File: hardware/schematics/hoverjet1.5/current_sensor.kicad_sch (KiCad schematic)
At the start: 6 parts, among them J5 -VIN, J6 +VIN, J7 Conn_01x06

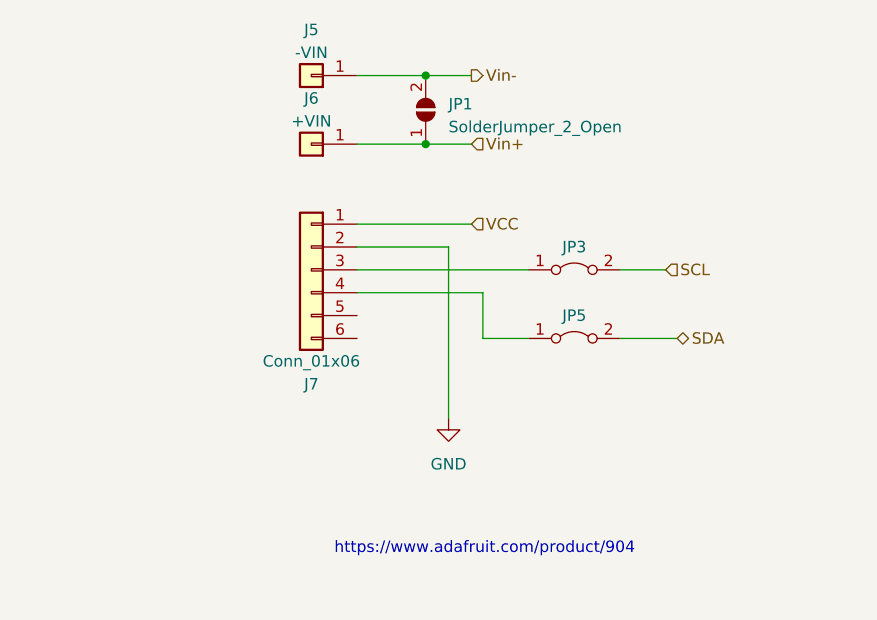
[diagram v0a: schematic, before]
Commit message: added adafruit current sense breakout
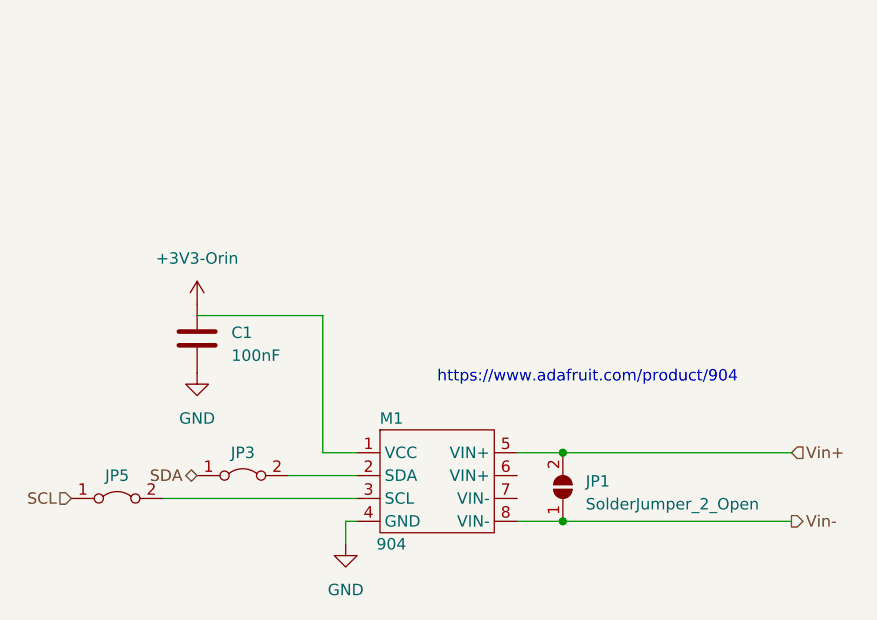
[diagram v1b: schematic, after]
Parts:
- removed J5: -VIN, symbol Connector_Generic:Conn_01x01
- removed J6: +VIN, symbol Connector_Generic:Conn_01x01
- removed J7: Conn_01x06, symbol Connector_Generic:Conn_01x06
- added C1: 100nF, Capacitor_SMD:C_0201_0603Metric, symbol Device:C
- added M1: 904, symbol hoverjet:904
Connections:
- net GND: now also C1.2, M1.4 (GND)
- net SCL: now also JP5.1 (A); no longer JP3.2 (B)
- net SDA: now also JP3.1 (A); no longer JP5.2 (B)
- net Vin+: now also JP1.2 (B), M1.5 (VIN+); no longer JP1.1 (A)
- net Vin-: now also JP1.1 (A), M1.8 (VIN-); no longer JP1.2 (B)
- new net: JP3.2 (B), M1.2 (SDA)
- new net: JP5.2 (B), M1.3 (SCL)
- new net +3V3-Orin: C1.1
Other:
- moved on the sheet: JP1, JP3, JP5

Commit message: syncing hardware changes
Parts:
- removed C1: 100nF, Capacitor_SMD:C_0201_0603Metric, symbol Device:C
- removed JP1: SolderJumper_2_Open, Jumper:SolderJumper-2_P1.3mm_Open_RoundedPad1.0x1.5mm, symbol Jumper:SolderJumper_2_Open
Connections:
- net +3V3-Orin: now also M1.1 (VCC)
- net Vin+: now also M1.6 (VIN+)
- net Vin-: now also M1.7 (VIN-)
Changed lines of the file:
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@@
 (kicad_sch (version 20230121) (generator eeschema)
   (paper "A4")
-  (junction (at 152.4 100.33) (diameter 0) (color 0 0 0 0)
+  (junction (at 151.13 100.33) (diameter 0) (color 0 0 0 0)
   )
-  (junction (at 152.4 107.95) (diameter 0) (color 0 0 0 0)
+  (junction (at 151.13 107.95) (diameter 0) (color 0 0 0 0)
+  )
+  (wire (pts (xy 151.13 100.33) (xy 177.8 100.33))
+    (stroke (width 0) (type default))
   )
   (wire (pts (xy 121.92 102.87) (xy 129.54 102.87))
     (stroke (width 0) (type default))
   )
-  (wire (pts (xy 111.76 85.09) (xy 125.73 85.09))
+  (wire (pts (xy 147.32 107.95) (xy 151.13 107.95))
     (stroke (width 0) (type default))
   )
-  (wire (pts (xy 147.32 107.95) (xy 152.4 107.95))
+  (wire (pts (xy 151.13 105.41) (xy 151.13 107.95))
+    (stroke (width 0) (type default))
+  )
+  (wire (pts (xy 147.32 102.87) (xy 151.13 102.87))
+    (stroke (width 0) (type default))
+  )
+  (wire (pts (xy 147.32 105.41) (xy 151.13 105.41))
     (stroke (width 0) (type default))
   )
@@
     (stroke (width 0) (type default))
   )
-  (wire (pts (xy 147.32 100.33) (xy 152.4 100.33))
+  (wire (pts (xy 147.32 100.33) (xy 151.13 100.33))
     (stroke (width 0) (type default))
   )
-  (wire (pts (xy 152.4 107.95) (xy 177.8 107.95))
+  (wire (pts (xy 151.13 107.95) (xy 177.8 107.95))
     (stroke (width 0) (type default))
   )
-  (wire (pts (xy 125.73 85.09) (xy 125.73 100.33))
+  (wire (pts (xy 151.13 100.33) (xy 151.13 102.87))
     (stroke (width 0) (type default))
   )
   (wire (pts (xy 107.95 105.41) (xy 129.54 105.41))
-    (stroke (width 0) (type default))
-  )
-  (wire (pts (xy 152.4 100.33) (xy 177.8 100.33))
     (stroke (width 0) (type default))
   )
@@
     )
   )
-  (symbol (lib_id "power:GND") (at 111.76 91.44 0) (unit 1)
+  (symbol (lib_id "hoverjet:+3V3-Orin") (at 125.73 100.33 0) (unit 1)
     (in_bom yes) (on_board yes) (dnp no) (fields_autoplaced)
-    (property "Reference" "#PWR08" (at 111.76 97.79 0)
+    (property "Reference" "#PWR019" (at 125.73 104.14 0)
       (effects (font (size 1.27 1.27)) hide)
     )
-    (property "Value" "GND" (at 111.76 96.52 0)
+    (property "Value" "+3V3-Orin" (at 125.73 95.25 0)
       (effects (font (size 1.27 1.27)))
     )
-    (property "Footprint" "" (at 111.76 91.44 0)
+    (property "Footprint" "" (at 125.73 100.33 0)
       (effects (font (size 1.27 1.27)) hide)
     )
-    (property "Datasheet" "" (at 111.76 91.44 0)
-      (effects (font (size 1.27 1.27)) hide)
-    )
-    (pin "1")
-    (instances
-      (project "hoverjet1.5"
-        (path "/667b3107-350e-4594-8aa7-7f2b7bfa6370/61ccea04-2db4-419f-a542-3a277e457f40/b686100f-0650-40a5-8577-84613a1e214b"
-          (reference "#PWR08") (unit 1)
-        )
-        (path "/667b3107-350e-4594-8aa7-7f2b7bfa6370/61ccea04-2db4-419f-a542-3a277e457f40/a21bb2a3-fb47-48f7-9a11-9f63725ae484"
-          (reference "#PWR014") (unit 1)
-        )
-      )
-    )
-  )
-  (symbol (lib_id "hoverjet:+3V3-Orin") (at 111.76 83.82 0) (unit 1)
-    (in_bom yes) (on_board yes) (dnp no) (fields_autoplaced)
-    (property "Reference" "#PWR019" (at 111.76 87.63 0)
-      (effects (font (size 1.27 1.27)) hide)
-    )
-    (property "Value" "+3V3-Orin" (at 111.76 78.74 0)
-      (effects (font (size 1.27 1.27)))
-    )
-    (property "Footprint" "" (at 111.76 83.82 0)
-      (effects (font (size 1.27 1.27)) hide)
-    )
-    (property "Datasheet" "" (at 111.76 83.82 0)
+    (property "Datasheet" "" (at 125.73 100.33 0)
       (effects (font (size 1.27 1.27)) hide)
     )
@@
     )
   )
-  (symbol (lib_id "Jumper:SolderJumper_2_Open") (at 152.4 104.14 90) (unit 1)
-    (in_bom yes) (on_board yes) (dnp no) (fields_autoplaced)
-    (property "Reference" "JP1" (at 154.94 103.505 90)
-      (effects (font (size 1.27 1.27)) (justify right))
-    )
-    (property "Value" "SolderJumper_2_Open" (at 154.94 106.045 90)
-      (effects (font (size 1.27 1.27)) (justify right))
-    )
-    (property "Footprint" "Jumper:SolderJumper-2_P1.3mm_Open_RoundedPad1.0x1.5mm" (at 152.4 104.14 0)
-      (effects (font (size 1.27 1.27)) hide)
-    )
-    (property "Datasheet" "~" (at 152.4 104.14 0)
-      (effects (font (size 1.27 1.27)) hide)
-    )
-    (pin "1")
-    (pin "2")
-    (instances
-      (project "hoverjet1.5"
-        (path "/667b3107-350e-4594-8aa7-7f2b7bfa6370/61ccea04-2db4-419f-a542-3a277e457f40/b686100f-0650-40a5-8577-84613a1e214b"
-          (reference "JP1") (unit 1)
-        )
-        (path "/667b3107-350e-4594-8aa7-7f2b7bfa6370/61ccea04-2db4-419f-a542-3a277e457f40/a21bb2a3-fb47-48f7-9a11-9f63725ae484"
-          (reference "JP2") (unit 1)
-        )
-      )
-    )
-  )
   (symbol (lib_id "Jumper:Jumper_2_Bridged") (at 102.87 105.41 0) (unit 1)
     (in_bom yes) (on_board yes) (dnp no)
@@
         )
       )
-    )
-  )
-  (symbol (lib_id "Device:C") (at 111.76 87.63 0) (unit 1)
-    (in_bom yes) (on_board yes) (dnp no) (fields_autoplaced)
-    (property "Reference" "C1" (at 115.57 86.995 0)
-      (effects (font (size 1.27 1.27)) (justify left))
-    )
-    (property "Value" "100nF" (at 115.57 89.535 0)
-      (effects (font (size 1.27 1.27)) (justify left))
-    )
-    (property "Footprint" "Capacitor_SMD:C_0201_0603Metric" (at 112.7252 91.44 0)
-      (effects (font (size 1.27 1.27)) hide)
-    )
-    (property "Datasheet" "~" (at 111.76 87.63 0)
-      (effects (font (size 1.27 1.27)) hide)
-    )
-    (property "PN" "CL10B104KB8NNNL" (at 111.76 87.63 0)
-      (effects (font (size 1.27 1.27)) hide)
-    )
-    (pin "1")
-    (pin "2")
-    (instances
-      (project "hoverjet1.5"
-        (path "/667b3107-350e-4594-8aa7-7f2b7bfa6370/61ccea04-2db4-419f-a542-3a277e457f40"
-          (reference "C1") (unit 1)
-        )
-        (path "/667b3107-350e-4594-8aa7-7f2b7bfa6370/61ccea04-2db4-419f-a542-3a277e457f40/b686100f-0650-40a5-8577-84613a1e214b"
-          (reference "C13") (unit 1)
-        )
-        (path "/667b3107-350e-4594-8aa7-7f2b7bfa6370/61ccea04-2db4-419f-a542-3a277e457f40/a21bb2a3-fb47-48f7-9a11-9f63725ae484"
-          (reference "C14") (unit 1)
-        )
-      )
